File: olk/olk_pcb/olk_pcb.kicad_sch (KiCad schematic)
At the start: 66 parts, among them SW0 SWITCH, SW1 SWITCH, SW10 SWITCH, SW11 SWITCH, SW12 SWITCH, SW13 SWITCH, SW14 SWITCH, SW15 SWITCH, SW16 SWITCH, SW17 SWITCH, SW18 SWITCH, SW19 SWITCH, SW2 SWITCH, SW20 SWITCH, SW21 SWITCH, SW22 SWITCH, SW23 SWITCH, SW24 SWITCH, SW25 SWITCH, SW26 SWITCH, SW27 SWITCH, SW28 SWITCH, SW29 SWITCH, SW3 SWITCH, SW30 SWITCH, SW31 SWITCH, SW32 SWITCH, SW33 SWITCH, SW34 SWITCH, SW35 SWITCH, SW36 SWITCH, SW37 SWITCH, SW38 SWITCH, SW39 SWITCH, SW4 SWITCH, SW40 SWITCH, SW41 SWITCH, SW42 SWITCH, SW43 SWITCH, SW44 SWITCH, SW45 SWITCH, SW46 SWITCH, SW47 SWITCH, SW48 SWITCH, SW49 SWITCH, SW5 SWITCH, SW50 SWITCH, SW51 SWITCH, SW52 SWITCH, SW53 SWITCH, SW54 SWITCH, SW55 SWITCH, SW6 SWITCH, SW7 SWITCH, SW8 SWITCH, SW9 SWITCH, U0 NICE!

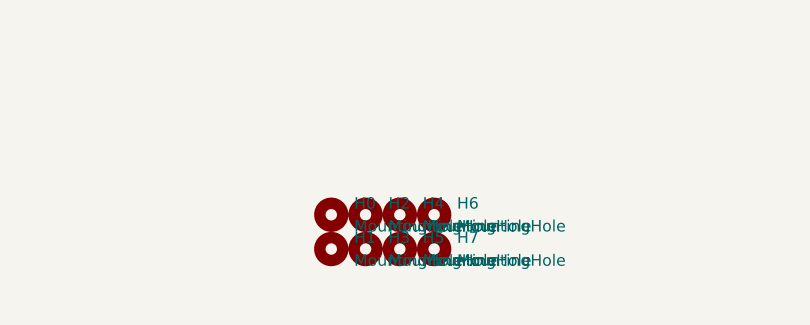
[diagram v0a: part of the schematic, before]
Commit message: Changed the shape of the olk_pcb.
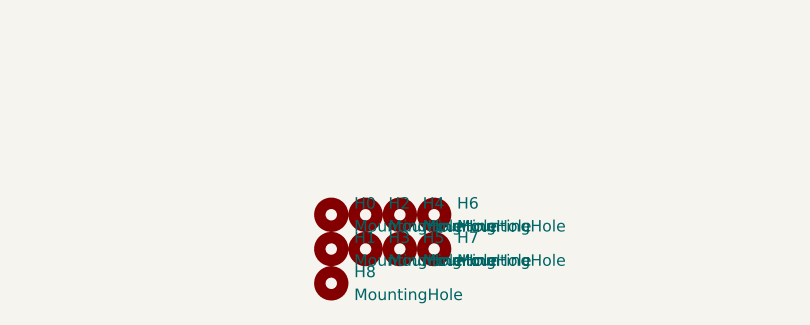
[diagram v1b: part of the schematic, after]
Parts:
- added H8: MountingHole, MountingHole:MountingHole_3.5mm, symbol Mechanical:MountingHole
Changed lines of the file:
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@@
+	)
+	(symbol
+		(lib_id "Mechanical:MountingHole")
+		(at 119.38 257.81 0)
+		(unit 1)
+		(body_style 1)
+		(exclude_from_sim no)
+		(in_bom yes)
+		(on_board yes)
+		(in_pos_files yes)
+		(dnp no)
+		(fields_autoplaced yes)
+		(property "Reference" "H8"
+			(at 121.92 256.54 0)
+			(show_name no)
+			(do_not_autoplace no)
+			(effects
+				(font
+					(size 1.27 1.27)
+				)
+				(justify left)
+			)
+		)
+		(property "Value" "MountingHole"
+			(at 121.92 259.08 0)
+			(show_name no)
+			(do_not_autoplace no)
+			(effects
+				(font
+					(size 1.27 1.27)
+				)
+				(justify left)
+			)
+		)
+		(property "Footprint" "MountingHole:MountingHole_3.5mm"
+			(at 119.38 257.81 0)
+			(hide yes)
+			(show_name no)
+			(do_not_autoplace no)
+			(effects
+				(font
+					(size 1.27 1.27)
+				)
+			)
+		)
+		(property "Datasheet" ""
+			(at 119.38 257.81 0)
+			(hide yes)
+			(show_name no)
+			(do_not_autoplace no)
+			(effects
+				(font
+					(size 1.27 1.27)
+				)
+			)
+		)
+		(property "Description" ""
+			(at 119.38 257.81 0)
+			(show_name no)
+			(do_not_autoplace no)
+			(effects
+				(font
+					(size 1.27 1.27)
+				)
+			)
+		)
+		(instances
+			(project "olk_pcb"
+				(path "/97127b28-60f4-45ff-835e-dccfbc833331"
+					(reference "H8")
+					(unit 1)
+				)
+			)
+		)
 	)
 	(symbol

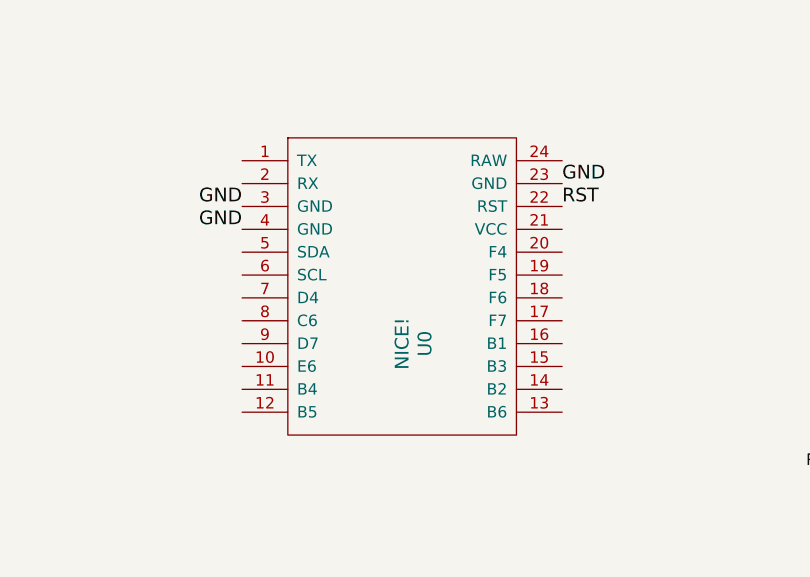
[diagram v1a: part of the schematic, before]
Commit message: Routed the olk.
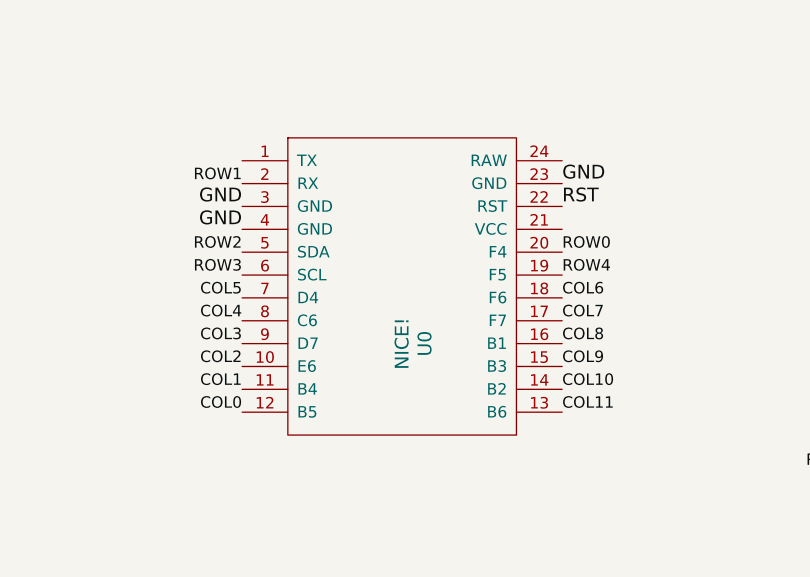
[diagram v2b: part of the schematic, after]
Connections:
- net COL0: now also U0.12 (B5)
- net COL1: now also U0.11 (B4)
- net COL10: now also U0.14 (B2)
- net COL11: now also U0.13 (B6)
- net COL2: now also U0.10 (E6)
- net COL3: now also U0.9 (D7)
- net COL4: now also U0.8 (C6)
- net COL5: now also U0.7 (D4)
- net COL6: now also U0.18 (F6)
- net COL7: now also U0.17 (F7)
- net COL8: now also U0.16 (B1)
- net COL9: now also U0.15 (B3)
- net ROW0: now also U0.20 (F4)
- net ROW1: now also U0.2 (RX)
- net ROW2: now also U0.5 (SDA)
- net ROW3: now also U0.6 (SCL)
- net ROW4: now also U0.19 (F5)
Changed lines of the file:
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@@
+		)
+	)
+	(label "COL3"
+		(at 101.6 210.82 180)
+		(effects
+			(font
+				(size 1.27 1.27)
+			)
+			(justify right bottom)
 		)
 	)
@@
 		)
 	)
+	(label "COL0"
+		(at 101.6 218.44 180)
+		(effects
+			(font
+				(size 1.27 1.27)
+			)
+			(justify right bottom)
+		)
+	)
 	(label "COL6"
 		(at 236.22 115.57 0)
@@
 		)
 	)
+	(label "ROW3"
+		(at 101.6 203.2 180)
+		(effects
+			(font
+				(size 1.27 1.27)
+			)
+			(justify right bottom)
+		)
+	)
 	(label "RST"
 		(at 167.64 224.79 180)
@@
 		)
 	)
+	(label "COL1"
+		(at 101.6 215.9 180)
+		(effects
+			(font
+				(size 1.27 1.27)
+			)
+			(justify right bottom)
+		)
+	)
 	(label "GND"
 		(at 101.6 198.12 180)
@@
 		)
 	)
+	(label "COL9"
+		(at 137.16 213.36 0)
+		(effects
+			(font
+				(size 1.27 1.27)
+			)
+			(justify left bottom)
+		)
+	)
+	(label "COL2"
+		(at 101.6 213.36 180)
+		(effects
+			(font
+				(size 1.27 1.27)
+			)
+			(justify right bottom)
+		)
+	)
+	(label "ROW0"
+		(at 137.16 200.66 0)
+		(effects
+			(font
+				(size 1.27 1.27)
+			)
+			(justify left bottom)
+		)
+	)
+	(label "COL5"
+		(at 101.6 205.74 180)
+		(effects
+			(font
+				(size 1.27 1.27)
+			)
+			(justify right bottom)
+		)
+	)
+	(label "ROW1"
+		(at 101.6 193.04 180)
+		(effects
+			(font
+				(size 1.27 1.27)
+			)
+			(justify right bottom)
+		)
+	)
 	(label "GND"
 		(at 177.8 224.79 0)
@@
 		)
 	)
+	(label "COL11"
+		(at 137.16 218.44 0)
+		(effects
+			(font
+				(size 1.27 1.27)
+			)
+			(justify left bottom)
+		)
+	)
 	(label "RST"
 		(at 137.16 195.58 0)
@@
 		)
 	)
+	(label "COL10"
+		(at 137.16 215.9 0)
+		(effects
+			(font
+				(size 1.27 1.27)
+			)
+			(justify left bottom)
+		)
+	)
 	(label "COL11"
 		(at 375.92 116.84 0)
@@
 		)
 	)
+	(label "COL4"
+		(at 101.6 208.28 180)
+		(effects
+			(font
+				(size 1.27 1.27)
+			)
+			(justify right bottom)
+		)
+	)
 	(label "COL5"
 		(at 195.58 116.84 0)
@@
 		)
 	)
+	(label "ROW4"
+		(at 137.16 203.2 0)
+		(effects
+			(font
+				(size 1.27 1.27)
+			)
+			(justify left bottom)
+		)
+	)
+	(label "COL8"
+		(at 137.16 210.82 0)
+		(effects
+			(font
+				(size 1.27 1.27)
+			)
+			(justify left bottom)
+		)
+	)
 	(label "COL10"
 		(at 347.98 116.84 0)
@@
 		(effects
 			(font
+				(size 1.27 1.27)
+			)
+			(justify left bottom)
+		)
+	)
+	(label "COL7"
+		(at 137.16 208.28 0)
+		(effects
+			(font
+				(size 1.27 1.27)
+			)
+			(justify left bottom)
+		)
+	)
+	(label "ROW2"
+		(at 101.6 200.66 180)
+		(effects
+			(font
+				(size 1.27 1.27)
+			)
+			(justify right bottom)
+		)
+	)
+	(label "COL6"
+		(at 137.16 205.74 0)
+		(effects
+			(font

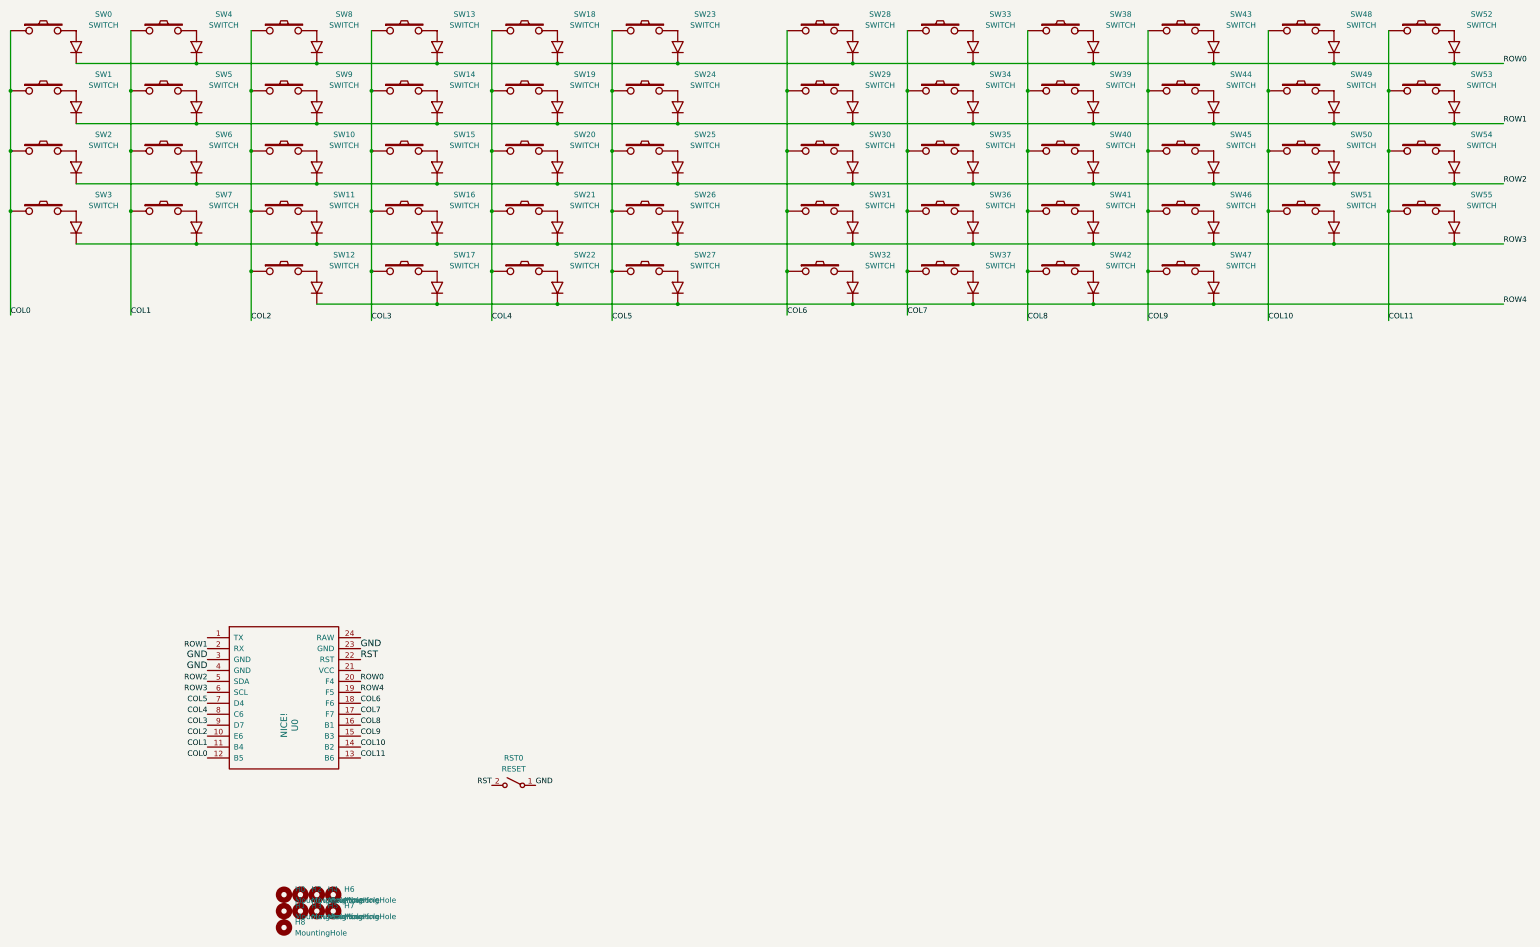
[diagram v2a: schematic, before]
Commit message: Switching olk to castellated pro micro footprint.
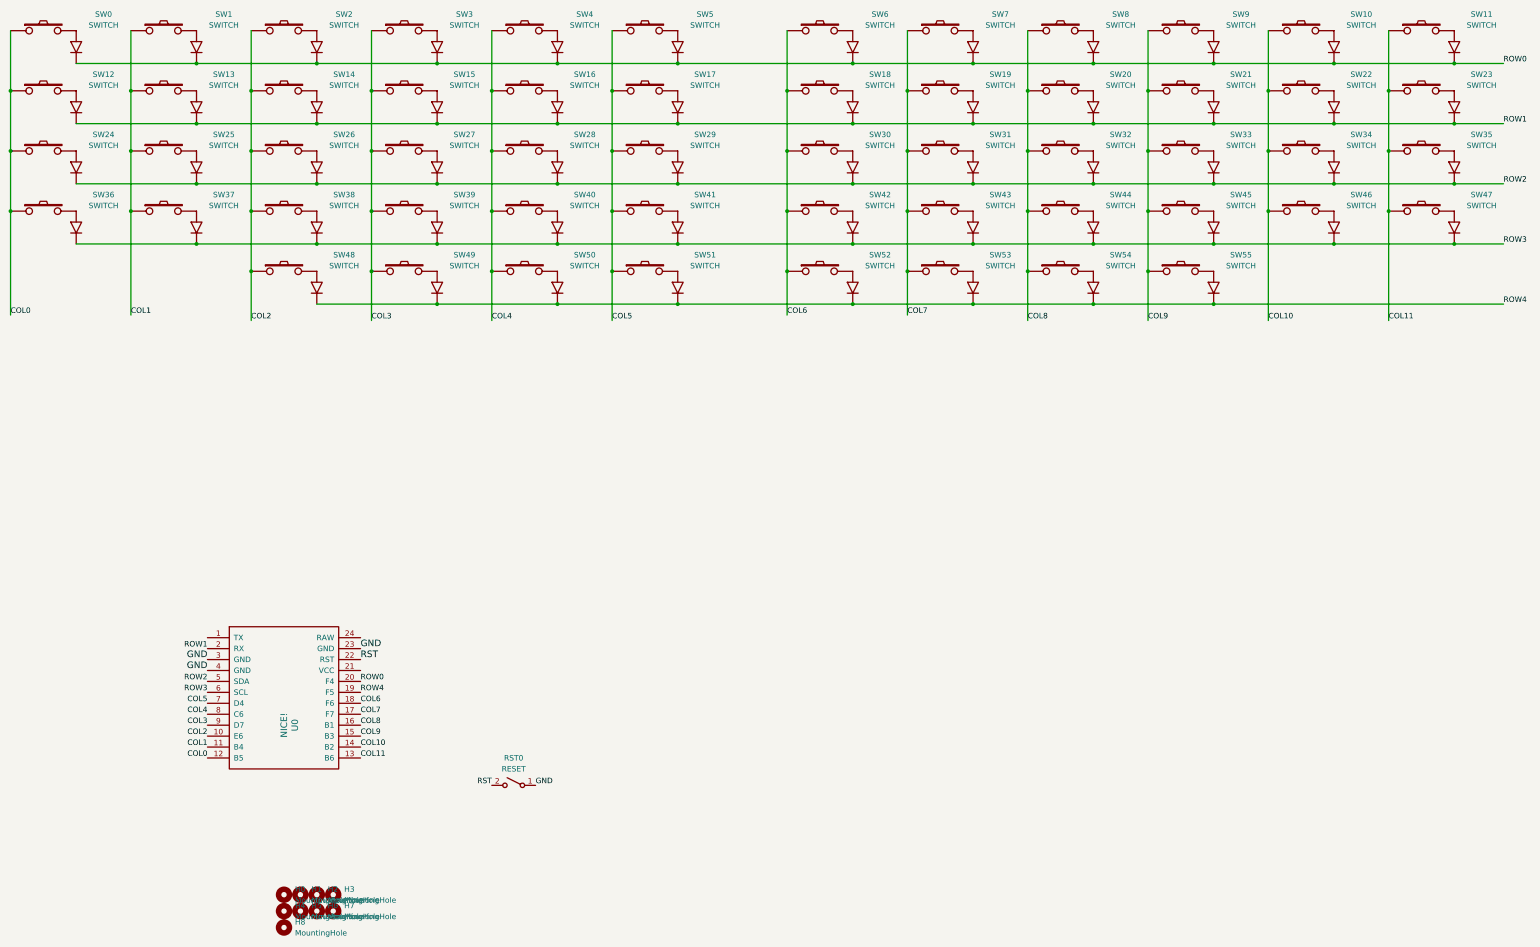
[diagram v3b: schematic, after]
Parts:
- U0: footprint footprints:nice!nano -> footprints:pro_micro_castellated
- renumbered H2 to H1, H4 to H2, H6 to H3, H1 to H4, H3 to H5, H5 to H6, SW4 to SW1, SW48 to SW10, SW52 to SW11, SW1 to SW12, SW5 to SW13, SW9 to SW14, SW14 to SW15, SW19 to SW16, SW24 to SW17, SW29 to SW18, SW34 to SW19, SW8 to SW2, SW39 to SW20, SW44 to SW21, SW49 to SW22, SW53 to SW23, SW2 to SW24, SW6 to SW25, SW10 to SW26, SW15 to SW27, SW20 to SW28, SW25 to SW29, SW13 to SW3, SW35 to SW31, SW40 to SW32, SW45 to SW33, SW50 to SW34, SW54 to SW35, SW3 to SW36, SW7 to SW37, SW11 to SW38, SW16 to SW39, SW18 to SW4, SW21 to SW40, SW26 to SW41, SW31 to SW42, SW36 to SW43, SW41 to SW44, SW46 to SW45, SW51 to SW46, SW55 to SW47, SW12 to SW48, SW17 to SW49, SW23 to SW5, SW22 to SW50, SW27 to SW51, SW32 to SW52, SW37 to SW53, SW42 to SW54, SW47 to SW55, SW28 to SW6, SW33 to SW7, SW38 to SW8, SW43 to SW9

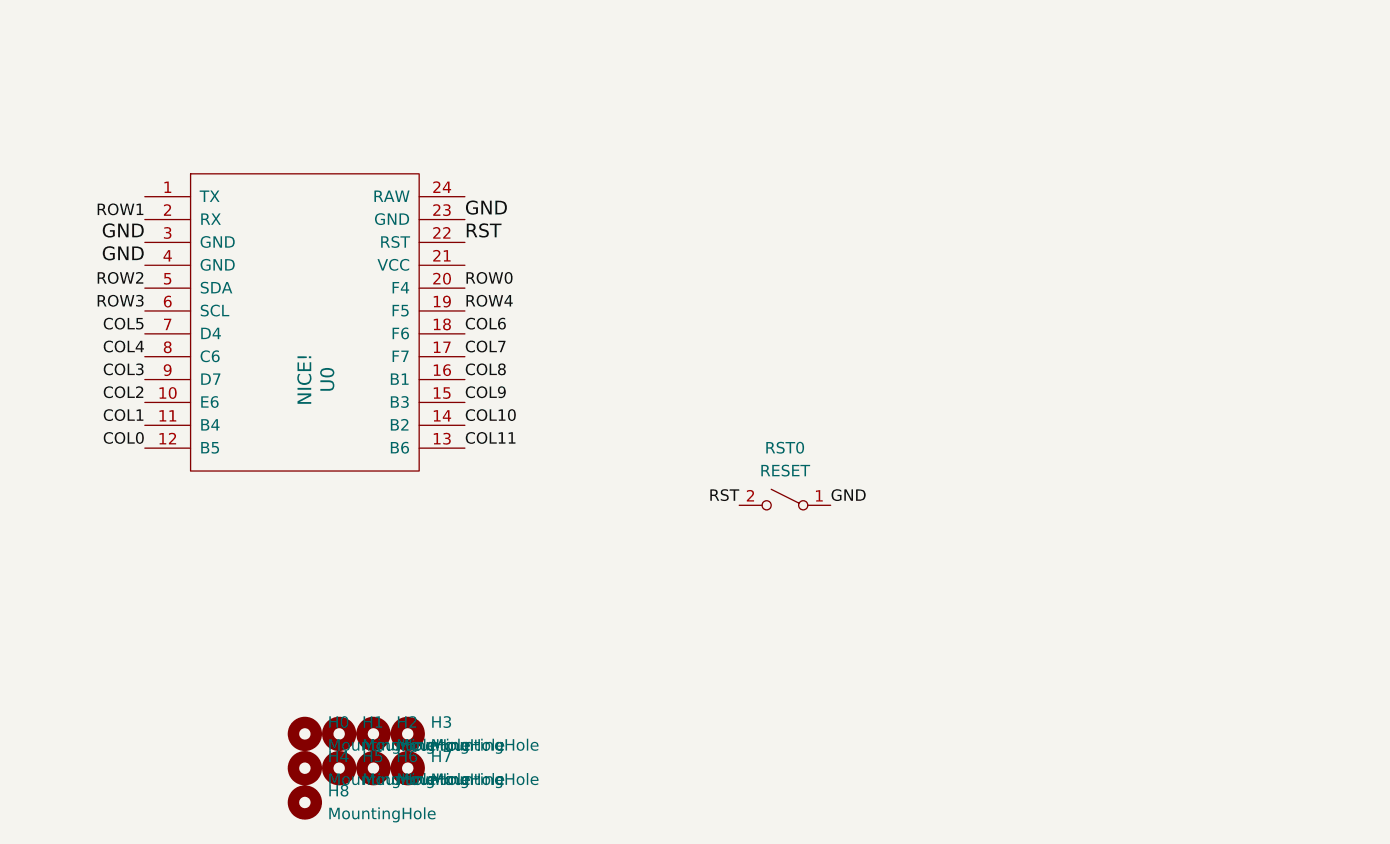
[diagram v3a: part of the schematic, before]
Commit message: Adding option for battery in olk_pcb.
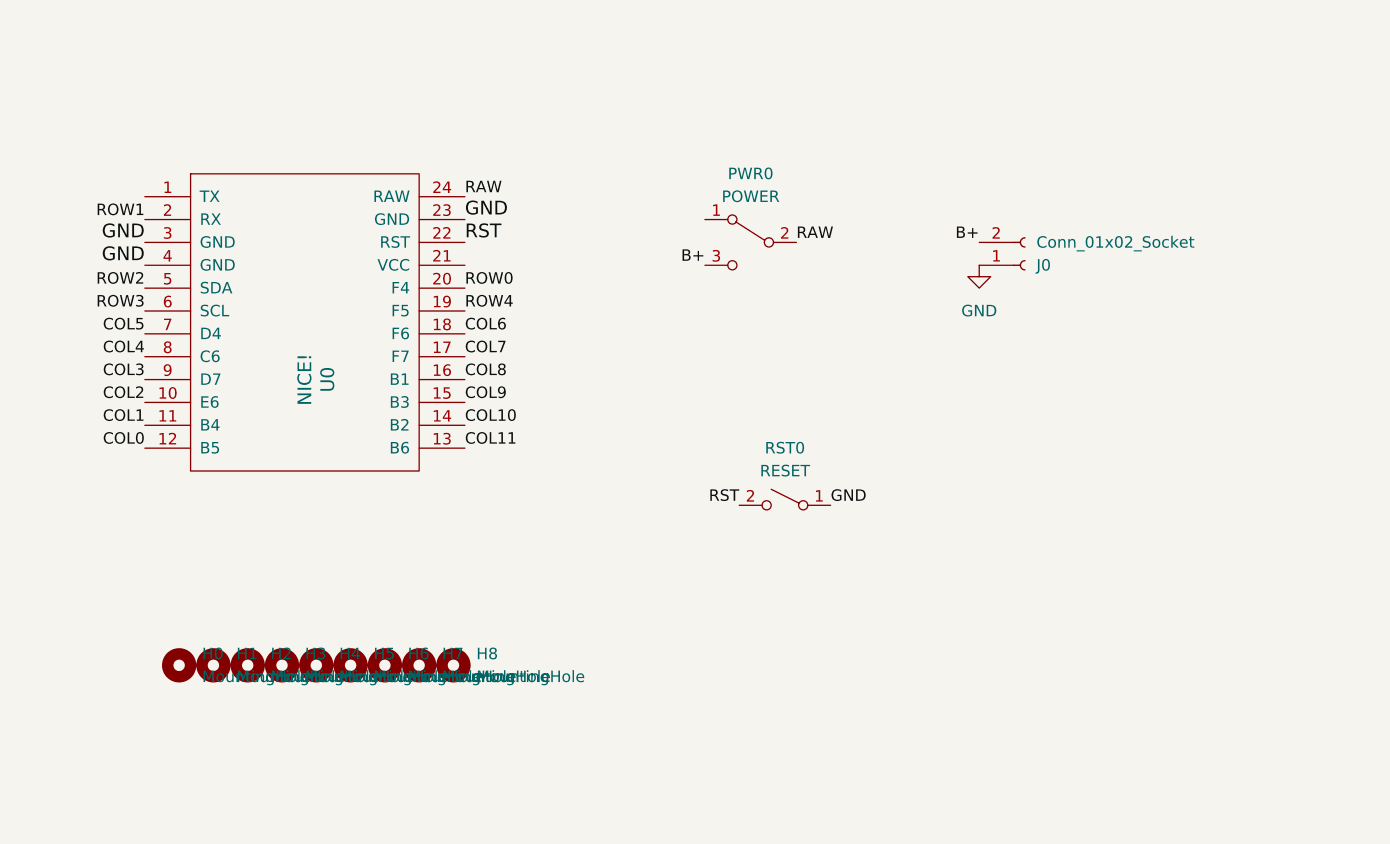
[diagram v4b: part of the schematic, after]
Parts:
- added J0: Conn_01x02_Socket, Connector_PinHeader_2.54mm:PinHeader_1x02_P2.54mm_Vertical, symbol Connector:Conn_01x02_Socket
- added PWR0: POWER, footprints:power_switch_1, symbol Switch:SW_SPDT
- renumbered H2 to H1, H5 to H2, H4 to H3, H1 to H4, H7 to H5, H3 to H6, H8 to H7, H6 to H8
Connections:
- net GND: now also J0.1 (Pin_1)
- net RAW: now reaches U0.24 (RAW)
- net RAW: now also PWR0.2 (B)
- new net B+: J0.2 (Pin_2), PWR0.3 (C)
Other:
- moved on the sheet: H0, H1, H2, H3, H4, H5, H6, H7, H8
